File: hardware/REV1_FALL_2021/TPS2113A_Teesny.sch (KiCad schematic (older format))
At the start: 6 parts, among them U201 TPS2113ADRBR

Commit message: start schematic
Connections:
- net GND: no longer C301.1, C302.1, U201.6 (IN2), U201.8 (IN1)
- new net IN1: C301.1, U201.8 (IN1)
- new net IN2: C302.1, U201.6 (IN2)
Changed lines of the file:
@@
-$Comp
-L power:GND #PWR?
-U 1 1 61AB466F
-P 3250 4200
-AR Path="/61AB466F" Ref="#PWR?"  Part="1"
-AR Path="/619AC3BC/61AB466F" Ref="#PWR0114"  Part="1"
-AR Path="/61A02CEE/61AB466F" Ref="#PWR0122"  Part="1"
-F 0 "#PWR0122" H 3250 3950 50  0001 C CNN
-F 1 "GND" H 3255 4027 50  0000 C CNN
-F 2 "" H 3250 4200 50  0001 C CNN
-F 3 "" H 3250 4200 50  0001 C CNN
-	1    3250 4200
-	1    0    0    -1
-$EndComp
 $Comp
 L power:GND #PWR?
@@
 F 3 "" H 4000 4200 50  0001 C CNN
 	1    4000 4200
-	1    0    0    -1
-$EndComp
-$Comp
-L power:GND #PWR?
-U 1 1 61AB467B
-P 4750 4200
-AR Path="/61AB467B" Ref="#PWR?"  Part="1"
-AR Path="/619AC3BC/61AB467B" Ref="#PWR0116"  Part="1"
-AR Path="/61A02CEE/61AB467B" Ref="#PWR0124"  Part="1"
-F 0 "#PWR0124" H 4750 3950 50  0001 C CNN
-F 1 "GND" H 4755 4027 50  0000 C CNN
-F 2 "" H 4750 4200 50  0001 C CNN
-F 3 "" H 4750 4200 50  0001 C CNN
-	1    4750 4200
 	1    0    0    -1
 $EndComp
@@
 	3250 2850 3250 3700
 Wire Wire Line
-	3250 3700 3250 4200
-Connection ~ 3250 3700
-Wire Wire Line
 	4750 2950 4750 3700
 Wire Wire Line
 	4550 3700 4750 3700
-Connection ~ 4750 3700
-Wire Wire Line
-	4750 3700 4750 4200
 Text HLabel 8100 3250 2    50   Output ~ 0
 STAT

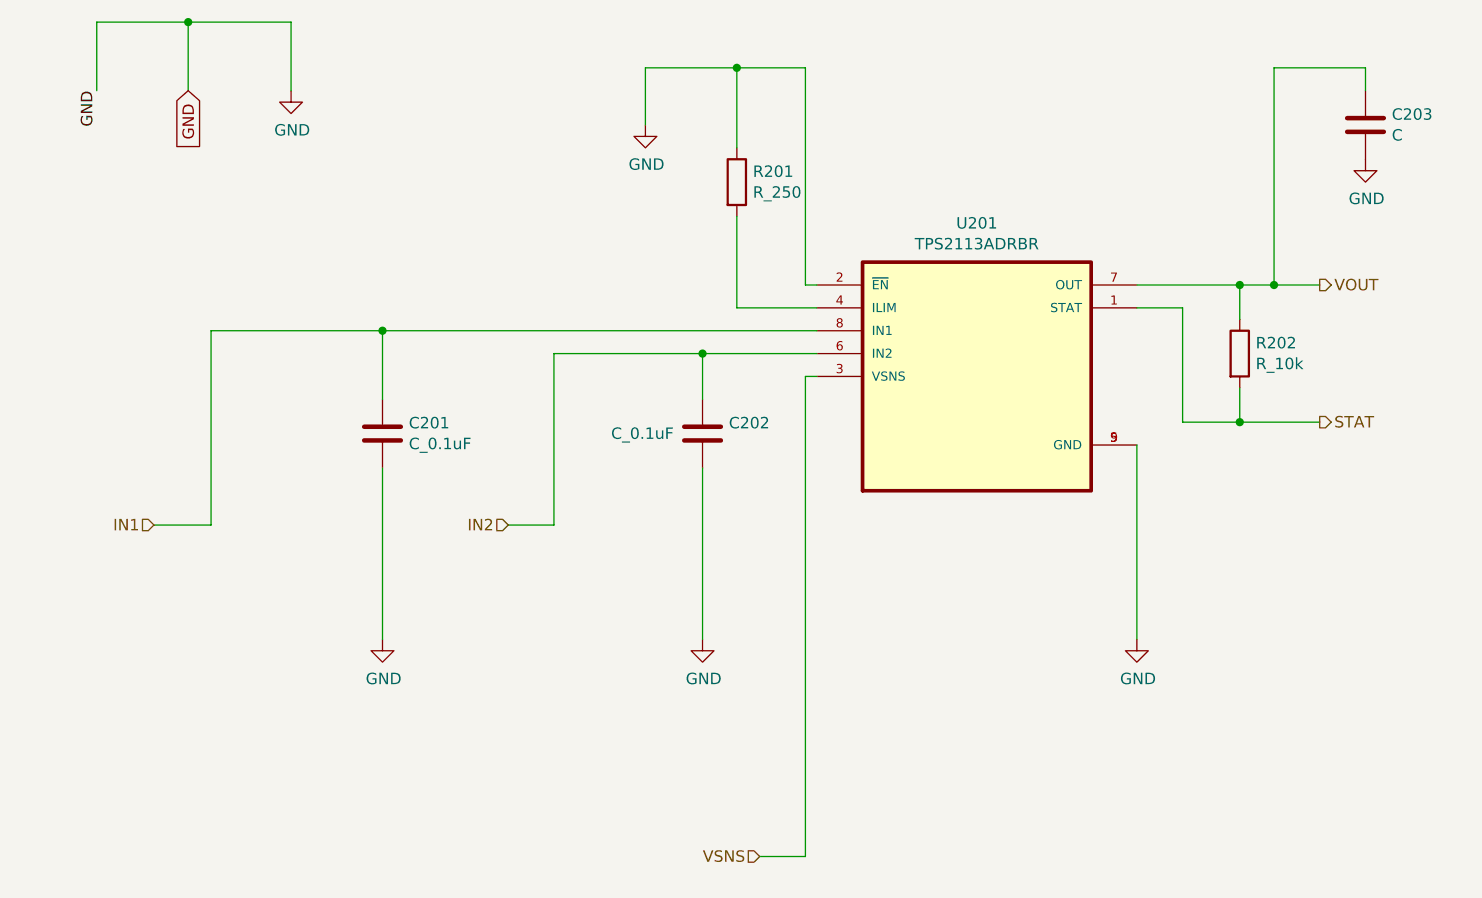
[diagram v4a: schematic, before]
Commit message: add LEDs to schematic
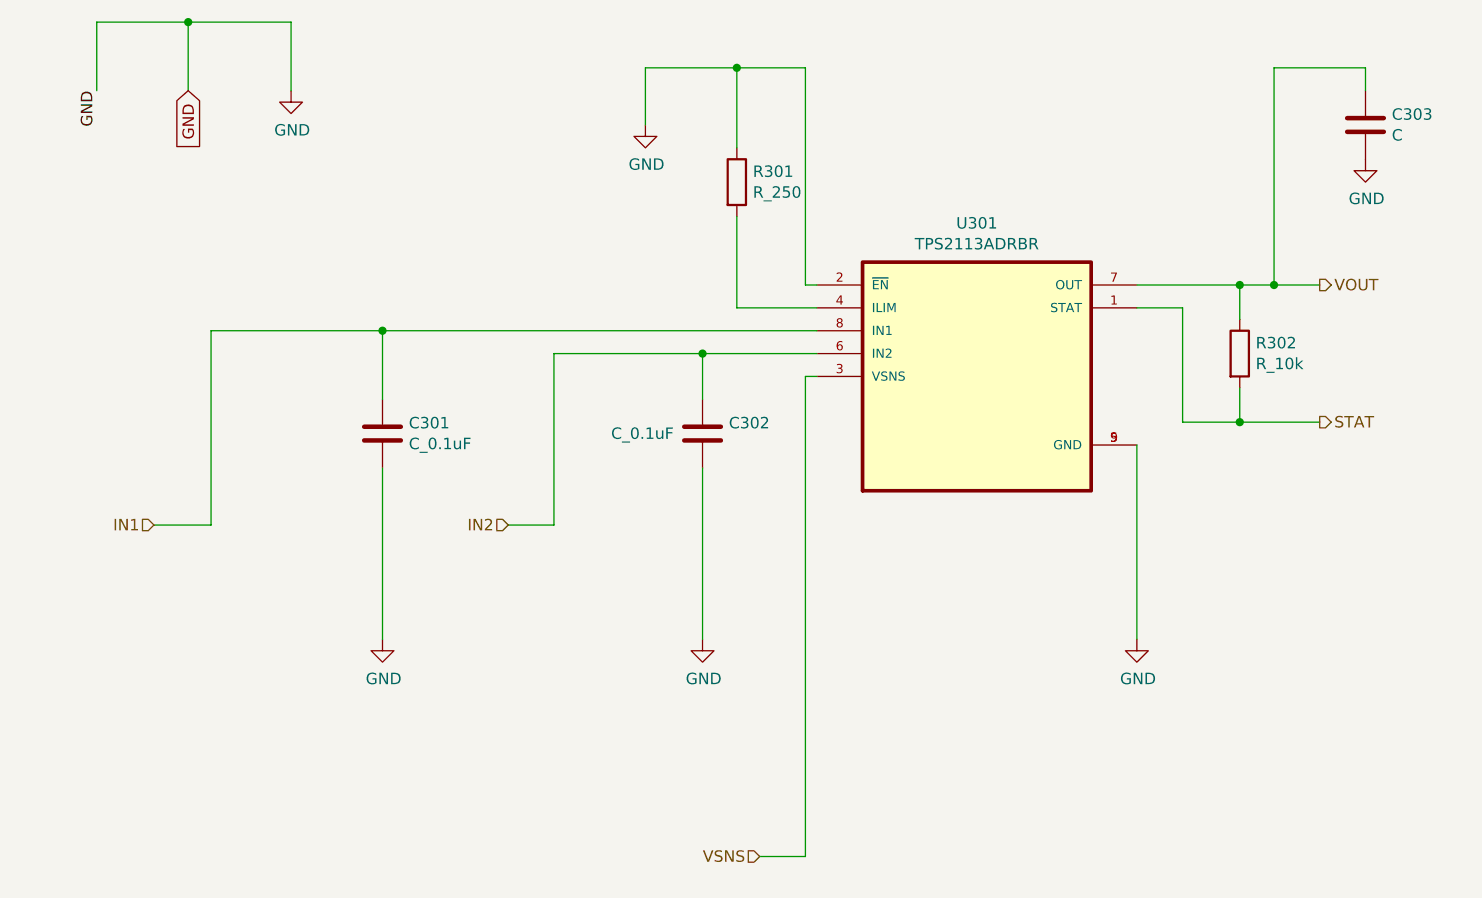
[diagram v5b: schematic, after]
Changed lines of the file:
@@
 AR Path="/61A02CEE/61AB462E" Ref="U201"  Part="1"
 AR Path="/619AC3BC/61AB462E" Ref="U301"  Part="1"
-F 0 "U201" H 6600 3720 50  0000 C CNN
+F 0 "U301" H 6600 3720 50  0000 C CNN
 F 1 "TPS2113ADRBR" H 6600 3629 50  0000 C CNN
 F 2 "footprints:TPS2113ADRBR" H 6600 3050 50  0001 L BNN
@@
 AR Path="/619AC3BC/61AB4644" Ref="C301"  Part="1"
 AR Path="/61A02CEE/61AB4644" Ref="C201"  Part="1"
-F 0 "C201" H 4115 3346 50  0000 L CNN
+F 0 "C301" H 4115 3346 50  0000 L CNN
 F 1 "C_0.1uF" H 4115 3255 50  0000 L CNN
 F 2 "Capacitor_SMD:C_0805_2012Metric_Pad1.18x1.45mm_HandSolder" H 4038 3150 50  0001 C CNN
@@
 AR Path="/619AC3BC/61AB464C" Ref="C302"  Part="1"
 AR Path="/61A02CEE/61AB464C" Ref="C202"  Part="1"
-F 0 "C202" H 5515 3346 50  0000 L CNN
+F 0 "C302" H 5515 3346 50  0000 L CNN
 F 1 "C_0.1uF" H 5000 3300 50  0000 L CNN
 F 2 "Capacitor_SMD:C_0805_2012Metric_Pad1.18x1.45mm_HandSolder" H 5438 3150 50  0001 C CNN
@@
 AR Path="/619AC3BC/61AB465E" Ref="R301"  Part="1"
 AR Path="/61A02CEE/61AB465E" Ref="R201"  Part="1"
-F 0 "R201" H 5620 2246 50  0000 L CNN
+F 0 "R301" H 5620 2246 50  0000 L CNN
 F 1 "R_250" H 5620 2155 50  0000 L CNN
 F 2 "Resistor_SMD:R_0805_2012Metric_Pad1.20x1.40mm_HandSolder" V 5480 2200 50  0001 C CNN
@@
 AR Path="/619AC3BC/61AB4669" Ref="#PWR0113"  Part="1"
 AR Path="/61A02CEE/61AB4669" Ref="#PWR0121"  Part="1"
-F 0 "#PWR0121" H 5150 1700 50  0001 C CNN
+F 0 "#PWR0113" H 5150 1700 50  0001 C CNN
 F 1 "GND" H 5155 1777 50  0000 C CNN
 F 2 "" H 5150 1950 50  0001 C CNN
@@
 AR Path="/619AC3BC/61AB4675" Ref="#PWR0115"  Part="1"
 AR Path="/61A02CEE/61AB4675" Ref="#PWR0123"  Part="1"
-F 0 "#PWR0123" H 4000 3950 50  0001 C CNN
+F 0 "#PWR0115" H 4000 3950 50  0001 C CNN
 F 1 "GND" H 4005 4027 50  0000 C CNN
 F 2 "" H 4000 4200 50  0001 C CNN
@@
 AR Path="/619AC3BC/61AB4681" Ref="#PWR0117"  Part="1"
 AR Path="/61A02CEE/61AB4681" Ref="#PWR0125"  Part="1"
-F 0 "#PWR0125" H 5400 3950 50  0001 C CNN
+F 0 "#PWR0117" H 5400 3950 50  0001 C CNN
 F 1 "GND" H 5405 4027 50  0000 C CNN
 F 2 "" H 5400 4200 50  0001 C CNN
@@
 AR Path="/619AC3BC/61AB4687" Ref="#PWR0118"  Part="1"
 AR Path="/61A02CEE/61AB4687" Ref="#PWR0126"  Part="1"
-F 0 "#PWR0126" H 7300 3950 50  0001 C CNN
+F 0 "#PWR0118" H 7300 3950 50  0001 C CNN
 F 1 "GND" H 7305 4027 50  0000 C CNN
 F 2 "" H 7300 4200 50  0001 C CNN
@@
 AR Path="/619AC3BC/61AB46B4" Ref="R302"  Part="1"
 AR Path="/61A02CEE/61AB46B4" Ref="R202"  Part="1"
-F 0 "R202" H 7820 2996 50  0000 L CNN
+F 0 "R302" H 7820 2996 50  0000 L CNN
 F 1 "R_10k" H 7820 2905 50  0000 L CNN
 F 2 "Resistor_SMD:R_0805_2012Metric_Pad1.20x1.40mm_HandSolder" V 7680 2950 50  0001 C CNN
@@
 AR Path="/619AC3BC/61AB46C3" Ref="C303"  Part="1"
 AR Path="/61A02CEE/61AB46C3" Ref="C203"  Part="1"
-F 0 "C203" H 8415 1996 50  0000 L CNN
+F 0 "C303" H 8415 1996 50  0000 L CNN
 F 1 "C" H 8415 1905 50  0000 L CNN
 F 2 "Capacitor_SMD:C_0805_2012Metric_Pad1.18x1.45mm_HandSolder" H 8338 1800 50  0001 C CNN
@@
 AR Path="/619AC3BC/61AB46CF" Ref="#PWR0119"  Part="1"
 AR Path="/61A02CEE/61AB46CF" Ref="#PWR0127"  Part="1"
-F 0 "#PWR0127" H 8300 1850 50  0001 C CNN
+F 0 "#PWR0119" H 8300 1850 50  0001 C CNN
 F 1 "GND" H 8305 1927 50  0000 C CNN
 F 2 "" H 8300 2100 50  0001 C CNN
@@
 AR Path="/619AC3BC/61ABB0D4" Ref="#PWR0120"  Part="1"
 AR Path="/61A02CEE/61ABB0D4" Ref="#PWR0128"  Part="1"
-F 0 "#PWR0128" H 3600 1550 50  0001 C CNN
+F 0 "#PWR0120" H 3600 1550 50  0001 C CNN
 F 1 "GND" H 3605 1627 50  0000 C CNN
 F 2 "" H 3600 1800 50  0001 C CNN

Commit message: add decoupling capacitor on Teensy VIN pin
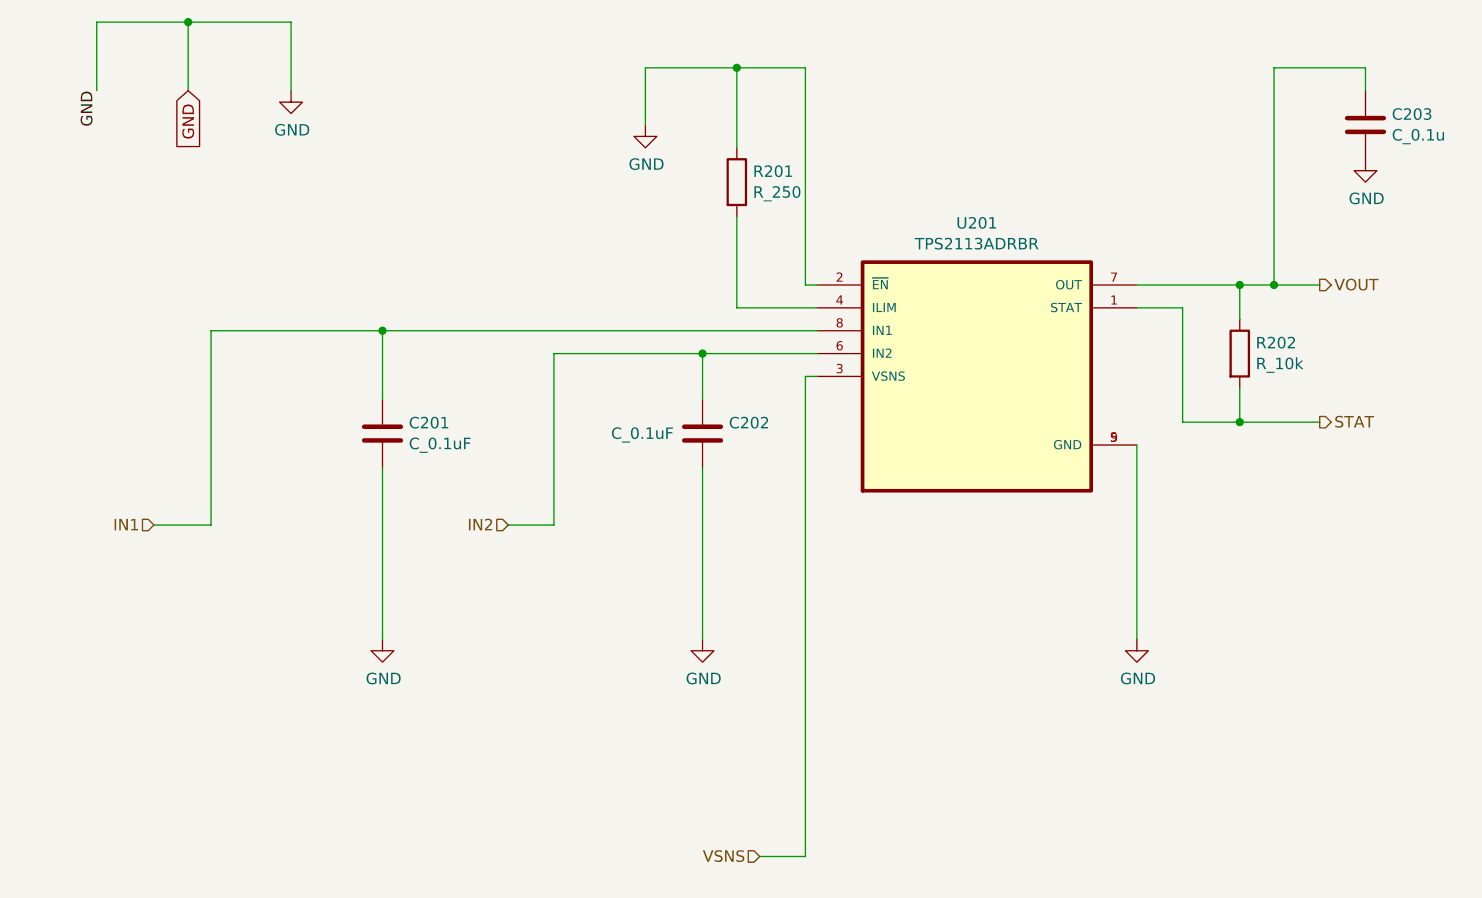
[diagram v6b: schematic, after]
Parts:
- C303: value C -> C_0.1u
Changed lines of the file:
@@
 AR Path="/61A02CEE/61AB462E" Ref="U201"  Part="1"
 AR Path="/619AC3BC/61AB462E" Ref="U301"  Part="1"
-F 0 "U301" H 6600 3720 50  0000 C CNN
+F 0 "U201" H 6600 3720 50  0000 C CNN
 F 1 "TPS2113ADRBR" H 6600 3629 50  0000 C CNN
 F 2 "footprints:TPS2113ADRBR" H 6600 3050 50  0001 L BNN
@@
 AR Path="/619AC3BC/61AB4644" Ref="C301"  Part="1"
 AR Path="/61A02CEE/61AB4644" Ref="C201"  Part="1"
-F 0 "C301" H 4115 3346 50  0000 L CNN
+F 0 "C201" H 4115 3346 50  0000 L CNN
 F 1 "C_0.1uF" H 4115 3255 50  0000 L CNN
 F 2 "Capacitor_SMD:C_0805_2012Metric_Pad1.18x1.45mm_HandSolder" H 4038 3150 50  0001 C CNN
@@
 AR Path="/619AC3BC/61AB464C" Ref="C302"  Part="1"
 AR Path="/61A02CEE/61AB464C" Ref="C202"  Part="1"
-F 0 "C302" H 5515 3346 50  0000 L CNN
+F 0 "C202" H 5515 3346 50  0000 L CNN
 F 1 "C_0.1uF" H 5000 3300 50  0000 L CNN
 F 2 "Capacitor_SMD:C_0805_2012Metric_Pad1.18x1.45mm_HandSolder" H 5438 3150 50  0001 C CNN
@@
 AR Path="/619AC3BC/61AB465E" Ref="R301"  Part="1"
 AR Path="/61A02CEE/61AB465E" Ref="R201"  Part="1"
-F 0 "R301" H 5620 2246 50  0000 L CNN
+F 0 "R201" H 5620 2246 50  0000 L CNN
 F 1 "R_250" H 5620 2155 50  0000 L CNN
 F 2 "Resistor_SMD:R_0805_2012Metric_Pad1.20x1.40mm_HandSolder" V 5480 2200 50  0001 C CNN
@@
 AR Path="/619AC3BC/61AB4669" Ref="#PWR0113"  Part="1"
 AR Path="/61A02CEE/61AB4669" Ref="#PWR0121"  Part="1"
-F 0 "#PWR0113" H 5150 1700 50  0001 C CNN
+F 0 "#PWR0121" H 5150 1700 50  0001 C CNN
 F 1 "GND" H 5155 1777 50  0000 C CNN
 F 2 "" H 5150 1950 50  0001 C CNN
@@
 AR Path="/619AC3BC/61AB4675" Ref="#PWR0115"  Part="1"
 AR Path="/61A02CEE/61AB4675" Ref="#PWR0123"  Part="1"
-F 0 "#PWR0115" H 4000 3950 50  0001 C CNN
+F 0 "#PWR0123" H 4000 3950 50  0001 C CNN
 F 1 "GND" H 4005 4027 50  0000 C CNN
 F 2 "" H 4000 4200 50  0001 C CNN
@@
 AR Path="/619AC3BC/61AB4681" Ref="#PWR0117"  Part="1"
 AR Path="/61A02CEE/61AB4681" Ref="#PWR0125"  Part="1"
-F 0 "#PWR0117" H 5400 3950 50  0001 C CNN
+F 0 "#PWR0125" H 5400 3950 50  0001 C CNN
 F 1 "GND" H 5405 4027 50  0000 C CNN
 F 2 "" H 5400 4200 50  0001 C CNN
@@
 AR Path="/619AC3BC/61AB4687" Ref="#PWR0118"  Part="1"
 AR Path="/61A02CEE/61AB4687" Ref="#PWR0126"  Part="1"
-F 0 "#PWR0118" H 7300 3950 50  0001 C CNN
+F 0 "#PWR0126" H 7300 3950 50  0001 C CNN
 F 1 "GND" H 7305 4027 50  0000 C CNN
 F 2 "" H 7300 4200 50  0001 C CNN
@@
 AR Path="/619AC3BC/61AB46B4" Ref="R302"  Part="1"
 AR Path="/61A02CEE/61AB46B4" Ref="R202"  Part="1"
-F 0 "R302" H 7820 2996 50  0000 L CNN
+F 0 "R202" H 7820 2996 50  0000 L CNN
 F 1 "R_10k" H 7820 2905 50  0000 L CNN
 F 2 "Resistor_SMD:R_0805_2012Metric_Pad1.20x1.40mm_HandSolder" V 7680 2950 50  0001 C CNN
@@
 AR Path="/619AC3BC/61AB46C3" Ref="C303"  Part="1"
 AR Path="/61A02CEE/61AB46C3" Ref="C203"  Part="1"
-F 0 "C303" H 8415 1996 50  0000 L CNN
-F 1 "C" H 8415 1905 50  0000 L CNN
+F 0 "C203" H 8415 1996 50  0000 L CNN
+F 1 "C_0.1u" H 8415 1905 50  0000 L CNN
 F 2 "Capacitor_SMD:C_0805_2012Metric_Pad1.18x1.45mm_HandSolder" H 8338 1800 50  0001 C CNN
 F 3 "~" H 8300 1950 50  0001 C CNN
@@
 AR Path="/619AC3BC/61AB46CF" Ref="#PWR0119"  Part="1"
 AR Path="/61A02CEE/61AB46CF" Ref="#PWR0127"  Part="1"
-F 0 "#PWR0119" H 8300 1850 50  0001 C CNN
+F 0 "#PWR0127" H 8300 1850 50  0001 C CNN
 F 1 "GND" H 8305 1927 50  0000 C CNN
 F 2 "" H 8300 2100 50  0001 C CNN
@@
 AR Path="/619AC3BC/61ABB0D4" Ref="#PWR0120"  Part="1"
 AR Path="/61A02CEE/61ABB0D4" Ref="#PWR0128"  Part="1"
-F 0 "#PWR0120" H 3600 1550 50  0001 C CNN
+F 0 "#PWR0128" H 3600 1550 50  0001 C CNN
 F 1 "GND" H 3605 1627 50  0000 C CNN
 F 2 "" H 3600 1800 50  0001 C CNN
